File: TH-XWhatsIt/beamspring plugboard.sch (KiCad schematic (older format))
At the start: 3 parts, among them J4 EXPANSION BEAMSPRING, J5 BEAMSPRING CONNECTOR, J6 EXPANSION BEAMSPRING

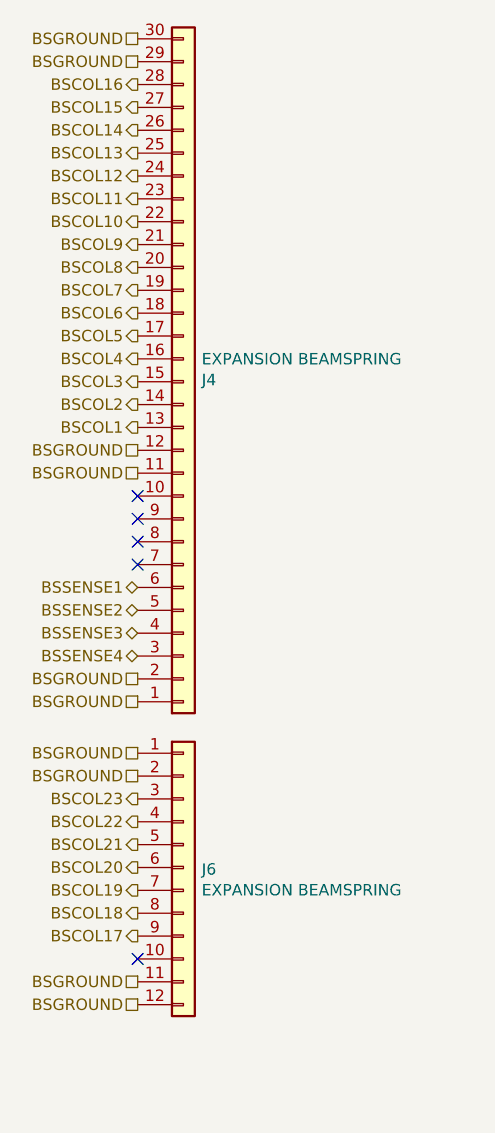
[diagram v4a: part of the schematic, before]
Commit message: Added cutout to the beamspring plugboard
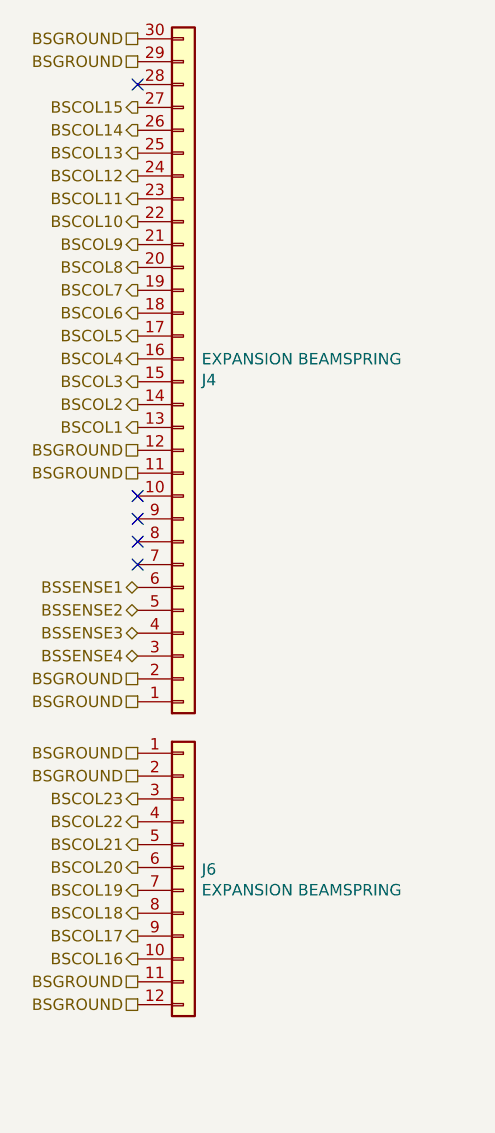
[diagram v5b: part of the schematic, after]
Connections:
- net BSCOL16: now also J6.10 (Pin_10); no longer J4.28 (Pin_28)
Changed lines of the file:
@@
 Text HLabel 2700 1625 0    50   Output ~ 0
 BSCOL12
-Text HLabel 2700 1525 0    50   Output ~ 0
-BSCOL13
-Text HLabel 2700 1425 0    50   Output ~ 0
-BSCOL14
-Text HLabel 2700 1325 0    50   Output ~ 0
-BSCOL15
-Text HLabel 2700 1225 0    50   Output ~ 0
-BSCOL16
 Text HLabel 2700 4950 0    50   Output ~ 0
 BSCOL17
@@
 Text Notes 3950 7750 0    50   ~ 0
 Copyright Rainy Day Plans.\nThis documentation describes Open Hardware and is licensed under the\nCERN OHL v. 1.2.\nYou may redistribute and modify this documentation under the terms of the\nCERN OHL v.1.2. (http://ohwr.org/cernohl). This documentation is distributed\nWITHOUT ANY EXPRESS OR IMPLIED WARRANTY, INCLUDING OF\nMERCHANTABILITY, SATISFACTORY QUALITY AND FITNESS FOR A\nPARTICULAR PURPOSE. Please see the CERN OHL v.1.2 for applicable\nconditions
-NoConn ~ 2700 5050
 Text HLabel 2700 2825 0    50   UnSpc ~ 0
 BSGROUND
@@
 NoConn ~ 2700 3225
 NoConn ~ 2700 3325
+Text HLabel 2700 1325 0    50   Output ~ 0
+BSCOL15
+Text HLabel 2700 1425 0    50   Output ~ 0
+BSCOL14
+Text HLabel 2700 1525 0    50   Output ~ 0
+BSCOL13
+Text HLabel 2700 5050 0    50   Output ~ 0
+BSCOL16
+NoConn ~ 2700 1225
 $EndSCHEMATC

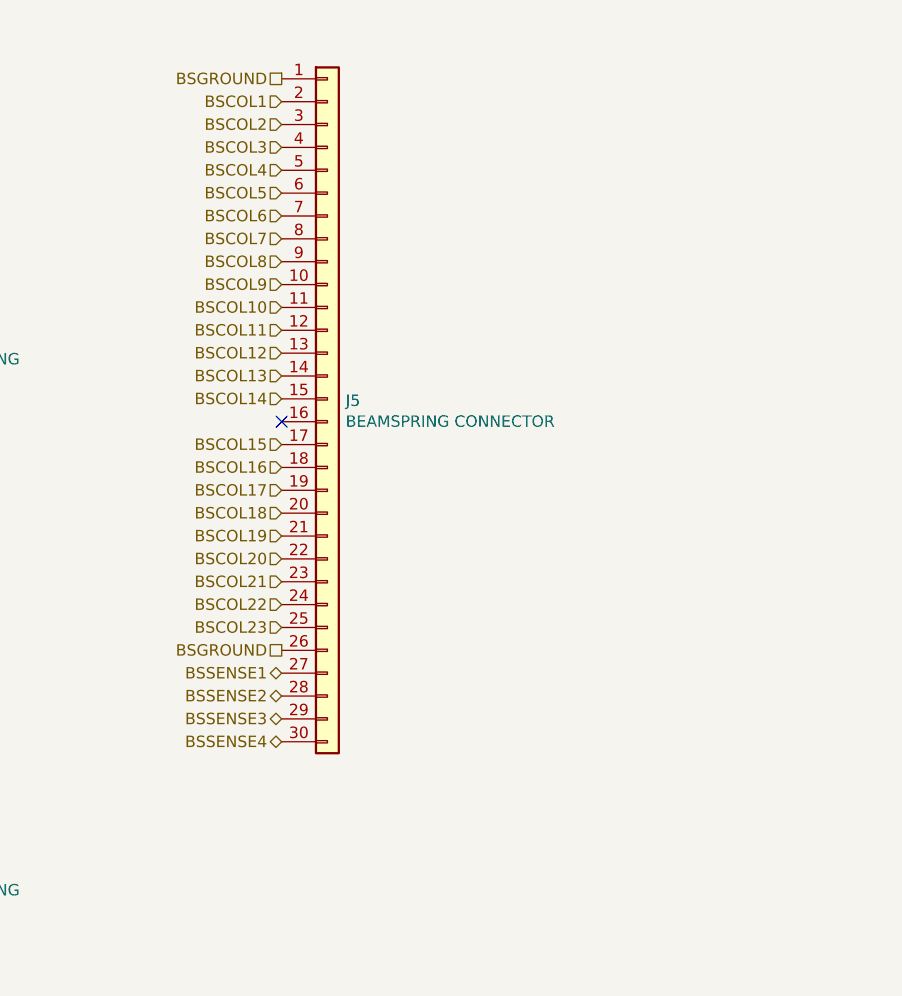
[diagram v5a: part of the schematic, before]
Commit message: use improved footprint, and improved pin ordering for beamspring
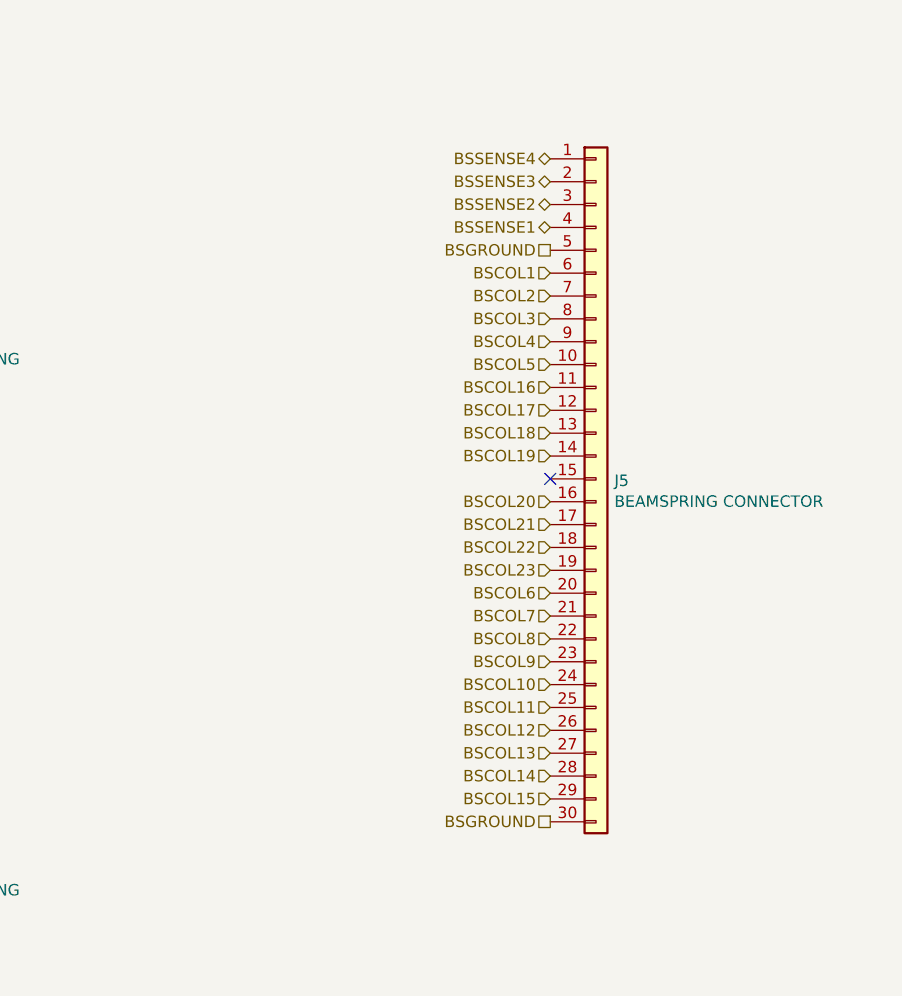
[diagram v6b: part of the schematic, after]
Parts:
- J5: footprint TH-XWhatsIt:30-pin-universal-beamspring-connector -> TH-XWhatsIt:30-pin-universal-beamspring-connector_v2
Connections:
- net BSCOL1: now also J5.6 (Pin_6); no longer J5.2 (Pin_2)
- net BSCOL10: now also J5.24 (Pin_24); no longer J5.11 (Pin_11)
- net BSCOL11: now also J5.25 (Pin_25); no longer J5.12 (Pin_12)
- net BSCOL12: now also J5.26 (Pin_26); no longer J5.13 (Pin_13)
- net BSCOL13: now also J5.27 (Pin_27); no longer J5.14 (Pin_14)
- net BSCOL14: now also J5.28 (Pin_28); no longer J5.15 (Pin_15)
- net BSCOL15: now also J5.29 (Pin_29); no longer J5.17 (Pin_17)
- net BSCOL16: now also J5.11 (Pin_11); no longer J5.18 (Pin_18)
- net BSCOL17: now also J5.12 (Pin_12); no longer J5.19 (Pin_19)
- net BSCOL18: now also J5.13 (Pin_13); no longer J5.20 (Pin_20)
- net BSCOL19: now also J5.14 (Pin_14); no longer J5.21 (Pin_21)
- net BSCOL2: now also J5.7 (Pin_7); no longer J5.3 (Pin_3)
- net BSCOL20: now also J5.16 (Pin_16); no longer J5.22 (Pin_22)
- net BSCOL21: now also J5.17 (Pin_17); no longer J5.23 (Pin_23)
- net BSCOL22: now also J5.18 (Pin_18); no longer J5.24 (Pin_24)
- net BSCOL23: now also J5.19 (Pin_19); no longer J5.25 (Pin_25)
- net BSCOL3: now also J5.8 (Pin_8); no longer J5.4 (Pin_4)
- net BSCOL4: now also J5.9 (Pin_9); no longer J5.5 (Pin_5)
- net BSCOL5: now also J5.10 (Pin_10); no longer J5.6 (Pin_6)
- net BSCOL6: now also J5.20 (Pin_20); no longer J5.7 (Pin_7)
- net BSCOL7: now also J5.21 (Pin_21); no longer J5.8 (Pin_8)
- net BSCOL8: now also J5.22 (Pin_22); no longer J5.9 (Pin_9)
- net BSCOL9: now also J5.23 (Pin_23); no longer J5.10 (Pin_10)
- net BSGROUND: now also J5.30 (Pin_30), J5.5 (Pin_5); no longer J5.1 (Pin_1), J5.26 (Pin_26)
- net BSSENSE1: now also J5.4 (Pin_4); no longer J5.27 (Pin_27)
- net BSSENSE2: now also J5.3 (Pin_3); no longer J5.28 (Pin_28)
- net BSSENSE3: now also J5.2 (Pin_2); no longer J5.29 (Pin_29)
- net BSSENSE4: now also J5.1 (Pin_1); no longer J5.30 (Pin_30)
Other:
- moved on the sheet: J5
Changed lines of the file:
@@
 	1    0    0    -1
 $EndComp
-NoConn ~ 5000 2700
+NoConn ~ 6175 2950
 Text HLabel 2700 2725 0    50   Output ~ 0
 BSCOL1
@@
 Text HLabel 2700 4350 0    50   Output ~ 0
 BSCOL23
-Text HLabel 5000 1300 0    50   Input ~ 0
+Text HLabel 6175 2050 0    50   Input ~ 0
 BSCOL1
-Text HLabel 5000 1400 0    50   Input ~ 0
+Text HLabel 6175 2150 0    50   Input ~ 0
 BSCOL2
-Text HLabel 5000 1500 0    50   Input ~ 0
+Text HLabel 6175 2250 0    50   Input ~ 0
 BSCOL3
-Text HLabel 5000 1600 0    50   Input ~ 0
+Text HLabel 6175 2350 0    50   Input ~ 0
 BSCOL4
-Text HLabel 5000 1700 0    50   Input ~ 0
+Text HLabel 6175 2450 0    50   Input ~ 0
 BSCOL5
-Text HLabel 5000 1800 0    50   Input ~ 0
+Text HLabel 6175 3450 0    50   Input ~ 0
 BSCOL6
-Text HLabel 5000 1900 0    50   Input ~ 0
+Text HLabel 6175 3550 0    50   Input ~ 0
 BSCOL7
-Text HLabel 5000 2000 0    50   Input ~ 0
+Text HLabel 6175 3650 0    50   Input ~ 0
 BSCOL8
-Text HLabel 5000 2100 0    50   Input ~ 0
+Text HLabel 6175 3750 0    50   Input ~ 0
 BSCOL9
-Text HLabel 5000 2200 0    50   Input ~ 0
+Text HLabel 6175 3850 0    50   Input ~ 0
 BSCOL10
-Text HLabel 5000 2300 0    50   Input ~ 0
+Text HLabel 6175 3950 0    50   Input ~ 0
 BSCOL11
-Text HLabel 5000 2400 0    50   Input ~ 0
+Text HLabel 6175 4050 0    50   Input ~ 0
 BSCOL12
-Text HLabel 5000 2500 0    50   Input ~ 0
+Text HLabel 6175 4150 0    50   Input ~ 0
 BSCOL13
-Text HLabel 5000 2600 0    50   Input ~ 0
+Text HLabel 6175 4250 0    50   Input ~ 0
 BSCOL14
-Text HLabel 5000 2800 0    50   Input ~ 0
+Text HLabel 6175 4350 0    50   Input ~ 0
 BSCOL15
-Text HLabel 5000 2900 0    50   Input ~ 0
+Text HLabel 6175 2550 0    50   Input ~ 0
 BSCOL16
-Text HLabel 5000 3000 0    50   Input ~ 0
+Text HLabel 6175 2650 0    50   Input ~ 0
 BSCOL17
-Text HLabel 5000 3100 0    50   Input ~ 0
+Text HLabel 6175 2750 0    50   Input ~ 0
 BSCOL18
-Text HLabel 5000 3200 0    50   Input ~ 0
+Text HLabel 6175 2850 0    50   Input ~ 0
 BSCOL19
-Text HLabel 5000 3300 0    50   Input ~ 0
+Text HLabel 6175 3050 0    50   Input ~ 0
 BSCOL20
-Text HLabel 5000 3400 0    50   Input ~ 0
+Text HLabel 6175 3150 0    50   Input ~ 0
 BSCOL21
-Text HLabel 5000 3500 0    50   Input ~ 0
+Text HLabel 6175 3250 0    50   Input ~ 0
 BSCOL22
-Text HLabel 5000 3600 0    50   Input ~ 0
+Text HLabel 6175 3350 0    50   Input ~ 0
 BSCOL23
 Text HLabel 2700 3425 0    50   BiDi ~ 0
@@
 Text HLabel 2700 3725 0    50   BiDi ~ 0
 BSSENSE4
-Text HLabel 5000 3800 0    50   BiDi ~ 0
+Text HLabel 6175 1850 0    50   BiDi ~ 0
 BSSENSE1
-Text HLabel 5000 3900 0    50   BiDi ~ 0
+Text HLabel 6175 1750 0    50   BiDi ~ 0
 BSSENSE2
-Text HLabel 5000 4000 0    50   BiDi ~ 0
+Text HLabel 6175 1650 0    50   BiDi ~ 0
 BSSENSE3
-Text HLabel 5000 4100 0    50   BiDi ~ 0
+Text HLabel 6175 1550 0    50   BiDi ~ 0
 BSSENSE4
 Text HLabel 2700 1025 0    50   UnSpc ~ 0
@@
 Text HLabel 2700 5250 0    50   UnSpc ~ 0
 BSGROUND
-Text HLabel 5000 3700 0    50   UnSpc ~ 0
+Text HLabel 6175 4450 0    50   UnSpc ~ 0
 BSGROUND
-Text HLabel 5000 1200 0    50   UnSpc ~ 0
+Text HLabel 6175 1950 0    50   UnSpc ~ 0
 BSGROUND
 Text Notes 3950 7750 0    50   ~ 0
@@
 L Connector_Generic:Conn_01x30 J?
 U 1 1 5F5D0CF1
-P 5200 2600
+P 6375 2950
 AR Path="/5F5D0CF1" Ref="J?"  Part="1"
 AR Path="/5E9772A5/5F5D0CF1" Ref="J5"  Part="1"
-F 0 "J5" H 5280 2592 50  0000 L CNN
-F 1 "BEAMSPRING CONNECTOR" H 5280 2501 50  0000 L CNN
-F 2 "TH-XWhatsIt:30-pin-universal-beamspring-connector" H 5200 2600 50  0001 C CNN
-F 3 "~" H 5200 2600 50  0001 C CNN
-	1    5200 2600
+F 0 "J5" H 6455 2942 50  0000 L CNN
+F 1 "BEAMSPRING CONNECTOR" H 6455 2851 50  0000 L CNN
+F 2 "TH-XWhatsIt:30-pin-universal-beamspring-connector_v2" H 6375 2950 50  0001 C CNN
+F 3 "~" H 6375 2950 50  0001 C CNN
+	1    6375 2950
 	1    0    0    -1
 $EndComp

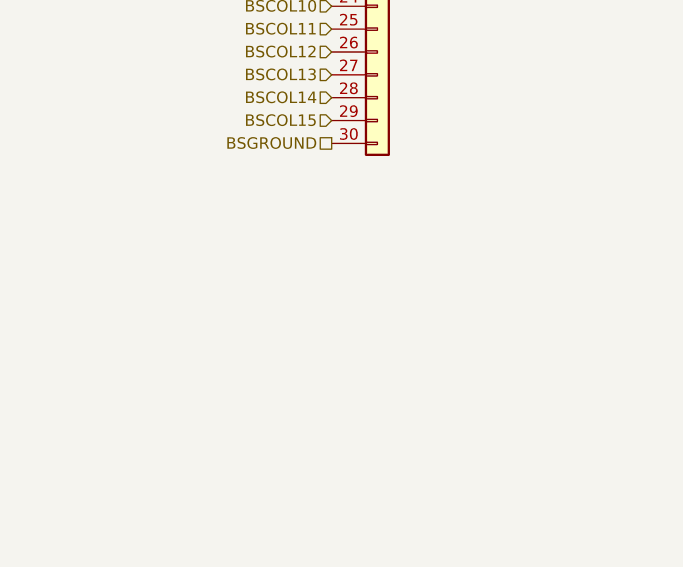
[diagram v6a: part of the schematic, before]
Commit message: Added beamspring mounting hole tab
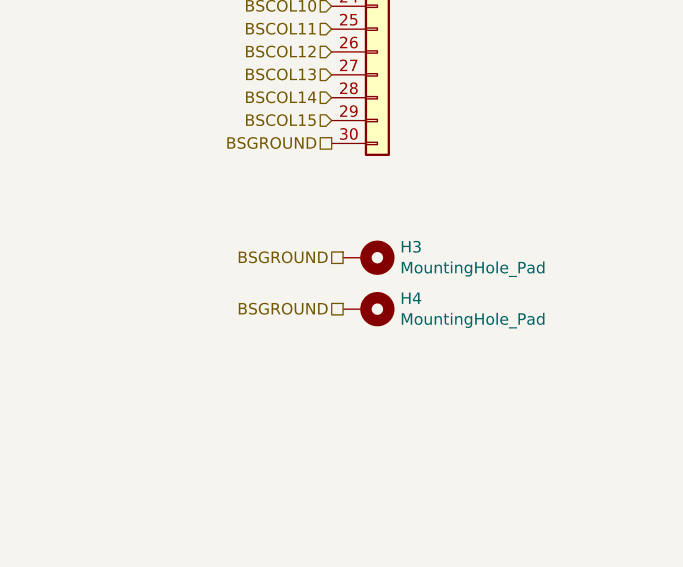
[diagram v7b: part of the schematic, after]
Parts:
- added H3: MountingHole_Pad, TH-XWhatsIt:BeamSpringGroundingMountingHole, symbol Mechanical:MountingHole_Pad
- added H4: MountingHole_Pad, MountingHole:MountingHole_4.5mm_Pad_Via, symbol Mechanical:MountingHole_Pad
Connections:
- net BSGROUND: now also H3.1, H4.1
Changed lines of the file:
@@
 BSCOL16
 NoConn ~ 2700 1225
+$Comp
+L Mechanical:MountingHole_Pad H3
+U 1 1 5F54034D
+P 6325 4950
+F 0 "H3" V 6371 5100 50  0000 L CNN
+F 1 "MountingHole_Pad" V 6280 5100 50  0000 L CNN
+F 2 "TH-XWhatsIt:BeamSpringGroundingMountingHole" H 6325 4950 50  0001 C CNN
+F 3 "~" H 6325 4950 50  0001 C CNN
+	1    6325 4950
+	0    1    -1   0
+$EndComp
+Text HLabel 6225 4950 0    50   UnSpc ~ 0
+BSGROUND
+$Comp
+L Mechanical:MountingHole_Pad H4
+U 1 1 5F554CE5
+P 6325 5175
+F 0 "H4" V 6371 5325 50  0000 L CNN
+F 1 "MountingHole_Pad" V 6280 5325 50  0000 L CNN
+F 2 "MountingHole:MountingHole_4.5mm_Pad_Via" H 6325 5175 50  0001 C CNN
+F 3 "~" H 6325 5175 50  0001 C CNN
+	1    6325 5175
+	0    1    -1   0
+$EndComp
+Text HLabel 6225 5175 0    50   UnSpc ~ 0
+BSGROUND
 $EndSCHEMATC
